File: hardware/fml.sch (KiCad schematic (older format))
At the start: 1 part, among them U1 Teensy3.6

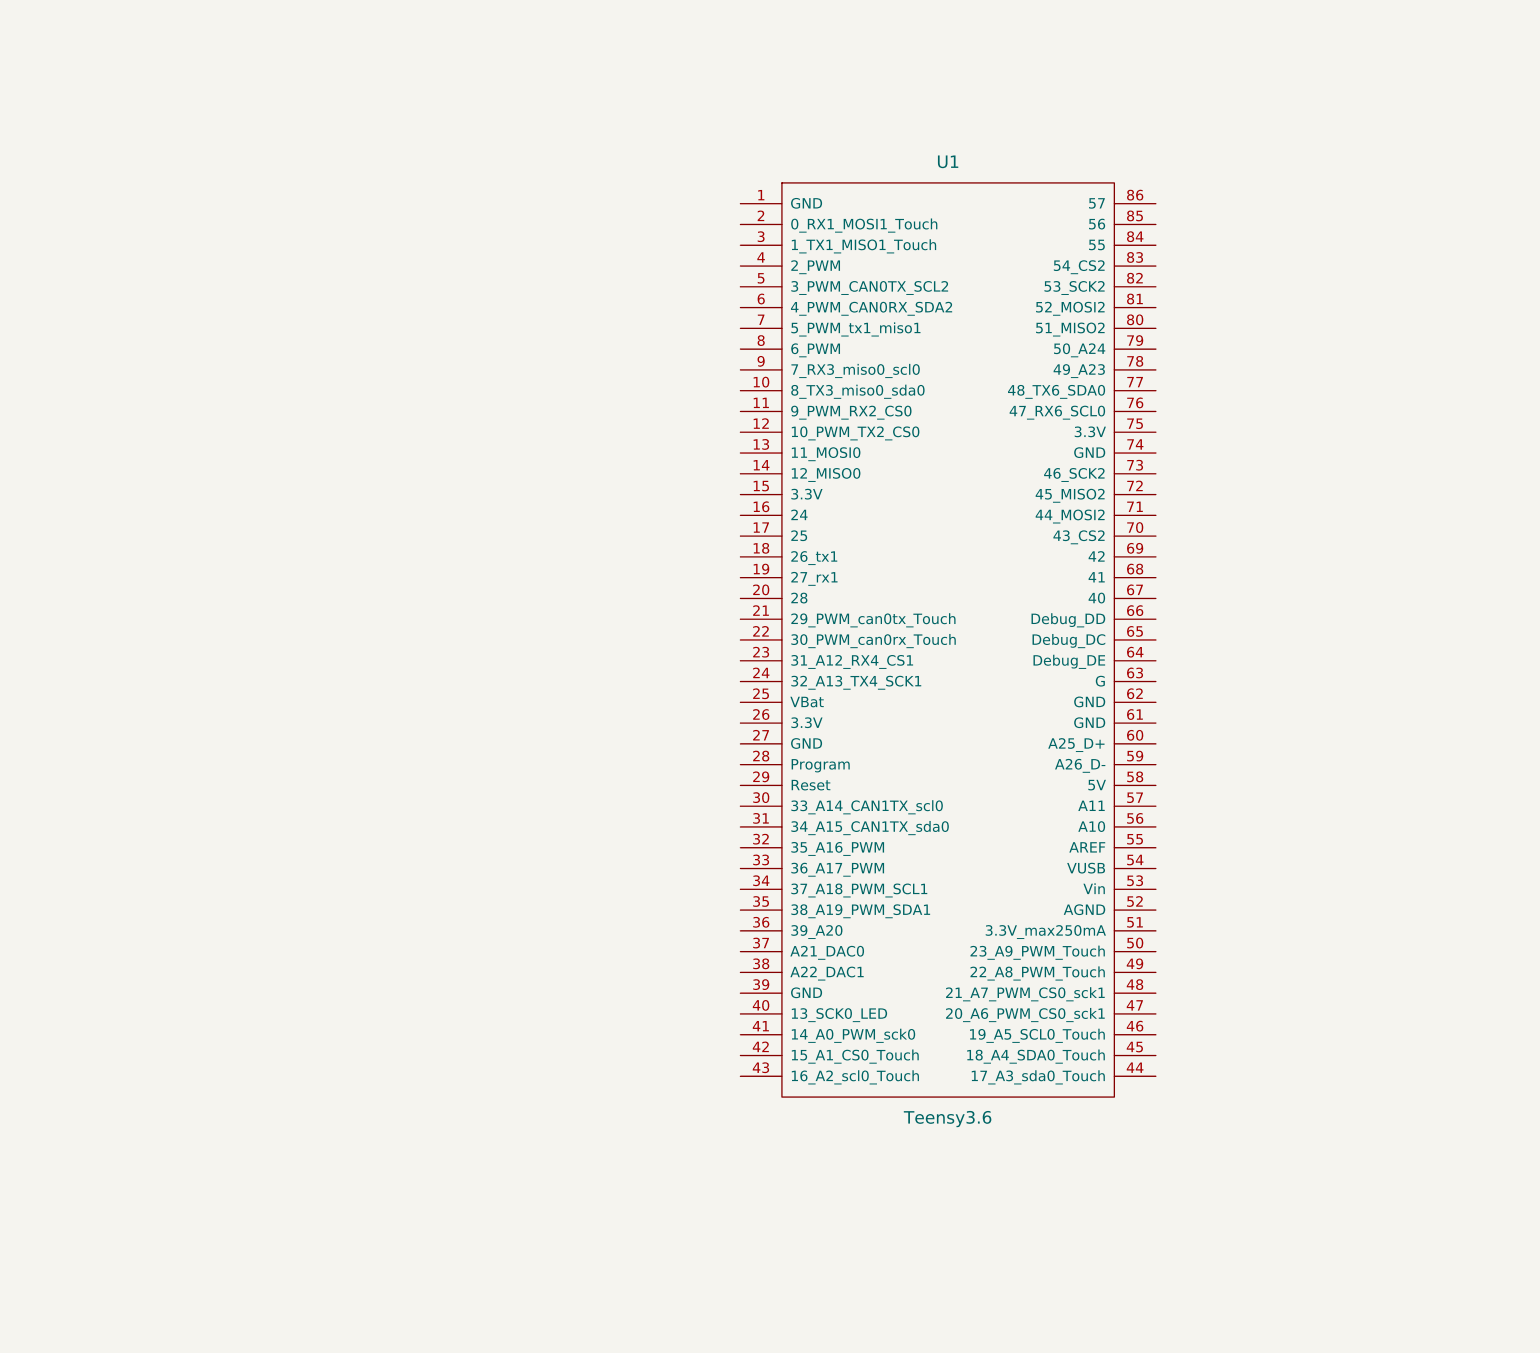
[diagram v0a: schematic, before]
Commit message: hooked up midi in and out
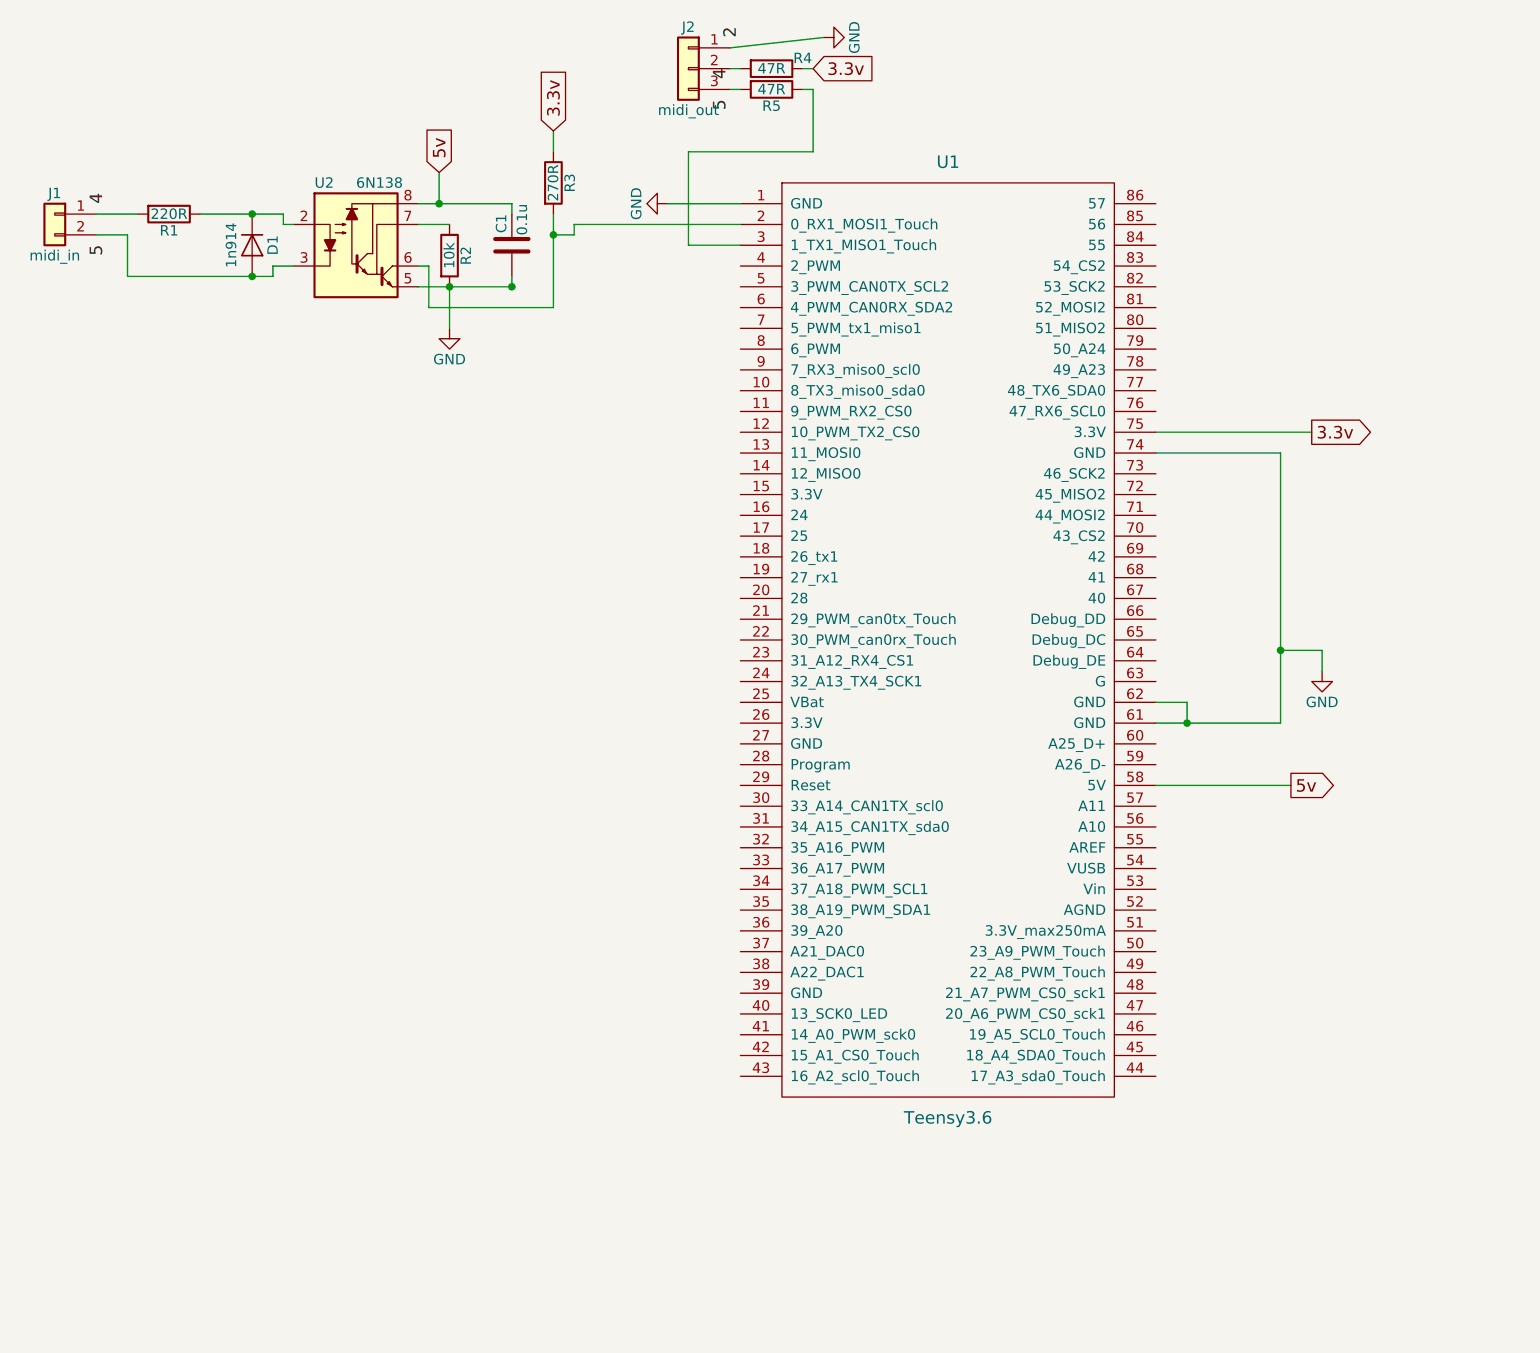
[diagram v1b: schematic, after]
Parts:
- added C1: 0.1u, Capacitors_ThroughHole:C_Disc_D5.0mm_W2.5mm_P2.50mm, symbol C
- added D1: 1n914, Diodes_ThroughHole:D_A-405_P7.62mm_Horizontal, symbol D
- added J1: midi_in, Pin_Headers:Pin_Header_Straight_1x02_Pitch2.54mm, symbol Conn_01x02
- added J2: midi_out, Pin_Headers:Pin_Header_Straight_1x03_Pitch2.54mm, symbol Conn_01x03
- added R1: 220R, xnorman:Resistor_Horizontal_RM10mm-xnorman, symbol R
- added R2: 10k, xnorman:Resistor_Horizontal_RM10mm-xnorman, symbol R
- added R3: 270R, xnorman:Resistor_Horizontal_RM10mm-xnorman, symbol R
- added R4, R5: 47R, xnorman:Resistor_Horizontal_RM10mm-xnorman, symbol R
- added U2: 6N138, Housings_DIP:DIP-8_W7.62mm, symbol 6N138
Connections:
- net GND: now reaches U1.1 (GND)
- net GND: now also U1.61 (GND), U1.62 (GND), U1.74 (GND), C1.1, J2.1 (Pin_1), R2.2, U2.5
- net at U1.2 (0_RX1_MOSI1_Touch): now also R3.2, U2.6
- net at U1.3 (1_TX1_MISO1_Touch): now also R5.1
- net 5v: now reaches U1.58 (5V)
- net 5v: now also C1.2, U2.8
- net 3.3v: now reaches U1.75 (3.3V)
- net 3.3v: now also R3.1, R4.1
- new net: D1.1 (K), R1.1, U2.2
- new net: D1.2 (A), J1.2 (Pin_2), U2.3
- new net: R2.1, U2.7
- new net: J1.1 (Pin_1), R1.2
- new net: J2.3 (Pin_3), R5.2
- new net: J2.2 (Pin_2), R4.2

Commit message: pcb updates
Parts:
- added J3, J4: pins, Pin_Headers:Pin_Header_Straight_1x24_Pitch2.54mm, symbol Conn_01x24
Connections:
- net 3.3v: now also U1.15 (3.3V), U1.26 (3.3V), J3.15 (Pin_15); no longer U1.75 (3.3V)
- net GND: now also U1.27 (GND), U1.39 (GND), J3.1 (Pin_1), J4.15 (Pin_15); no longer U1.74 (GND)
- net at U1.10 (8_TX3_miso0_sda0): now also J3.10 (Pin_10)
- net at U1.11 (9_PWM_RX2_CS0): now also J3.11 (Pin_11)
- net at U1.12 (10_PWM_TX2_CS0): now also J3.12 (Pin_12)
- net at U1.13 (11_MOSI0): now also J3.13 (Pin_13)
- net at U1.14 (12_MISO0): now also J3.14 (Pin_14)
- net at U1.16 (24): now also J3.16 (Pin_16)
- net at U1.17 (25): now also J3.17 (Pin_17)
- net at U1.18 (26_tx1): now also J3.18 (Pin_18)
- net at U1.19 (27_rx1): now also J3.19 (Pin_19)
- net at R3.2, U1.2 (0_RX1_MOSI1_Touch), U2.6: now also J3.2 (Pin_2)
- net at U1.20 (28): now also J3.20 (Pin_20)
- net at U1.21 (29_PWM_can0tx_Touch): now also J3.21 (Pin_21)
- net at U1.22 (30_PWM_can0rx_Touch): now also J3.22 (Pin_22)
- net at U1.23 (31_A12_RX4_CS1): now also J3.23 (Pin_23)
- net at U1.24 (32_A13_TX4_SCK1): now also J3.24 (Pin_24)
- net at R5.1, U1.3 (1_TX1_MISO1_Touch): now also J3.3 (Pin_3)
- net at U1.30 (33_A14_CAN1TX_scl0): now also J4.24 (Pin_24)
- net at U1.31 (34_A15_CAN1TX_sda0): now also J4.23 (Pin_23)
- net at U1.32 (35_A16_PWM): now also J4.22 (Pin_22)
- net at U1.33 (36_A17_PWM): now also J4.21 (Pin_21)
- net at U1.34 (37_A18_PWM_SCL1): now also J4.20 (Pin_20)
- net at U1.35 (38_A19_PWM_SDA1): now also J4.19 (Pin_19)
- net at U1.36 (39_A20): now also J4.18 (Pin_18)
- net at U1.37 (A21_DAC0): now also J4.17 (Pin_17)
- net at U1.38 (A22_DAC1): now also J4.16 (Pin_16)
- net at U1.4 (2_PWM): now also J3.4 (Pin_4)
- net at U1.40 (13_SCK0_LED): now also J4.14 (Pin_14)
- net at U1.41 (14_A0_PWM_sck0): now also J4.13 (Pin_13)
- net at U1.42 (15_A1_CS0_Touch): now also J4.12 (Pin_12)
- net at U1.43 (16_A2_scl0_Touch): now also J4.11 (Pin_11)
- net at U1.44 (17_A3_sda0_Touch): now also J4.10 (Pin_10)
- net at U1.45 (18_A4_SDA0_Touch): now also J4.9 (Pin_9)
- net at U1.46 (19_A5_SCL0_Touch): now also J4.8 (Pin_8)
- net at U1.47 (20_A6_PWM_CS0_sck1): now also J4.7 (Pin_7)
- net at U1.48 (21_A7_PWM_CS0_sck1): now also J4.6 (Pin_6)
- net at U1.49 (22_A8_PWM_Touch): now also J4.5 (Pin_5)
- net at U1.5 (3_PWM_CAN0TX_SCL2): now also J3.5 (Pin_5)
- net at U1.50 (23_A9_PWM_Touch): now also J4.4 (Pin_4)
- net at U1.51 (3.3V_max250mA): now also J4.3 (Pin_3)
- net at U1.52 (AGND): now also J4.2 (Pin_2)
- net at U1.53 (Vin): now also J4.1 (Pin_1)
- net at U1.6 (4_PWM_CAN0RX_SDA2): now also J3.6 (Pin_6)
- net at U1.7 (5_PWM_tx1_miso1): now also J3.7 (Pin_7)
- net at U1.8 (6_PWM): now also J3.8 (Pin_8)
- net at U1.9 (7_RX3_miso0_scl0): now also J3.9 (Pin_9)
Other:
- moved on the sheet: J2, R4, R5, U1
